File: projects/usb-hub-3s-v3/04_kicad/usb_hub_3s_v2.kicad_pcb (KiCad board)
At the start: 4 copper layers, 130 x 92 mm, 114 parts, among them J1 C98732, J2 C503996, J3 C503996, J4 C503996, J5 C5337088, Q1 C2760089, Q2 C404363, Q3 C404363, Q4 C404363, Q5 C404363, Q6 C2760089, Q7 C78284, SW1 C2939728, U10 C7519, U11 C13755, U12 C7519, U2 C13755, U3 C130056, U4 C130056, U5 C130056, U6 C473910, U7 C473910, U8 C7519, U9 C7519

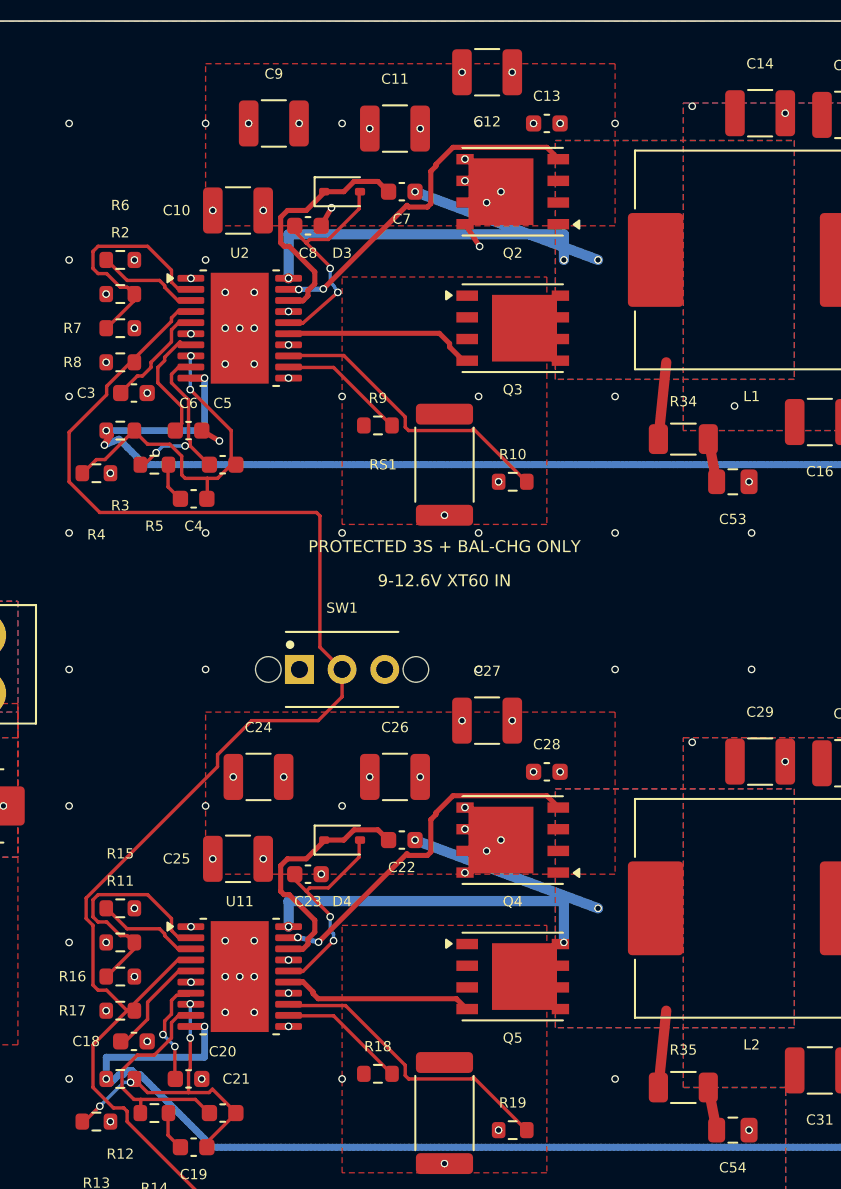
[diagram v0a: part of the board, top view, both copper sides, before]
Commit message: usb-hub-3s-v3 v1.3 gate (ii-b): R30 wrong-part fix (C25803) + full regen [source commit S]
R30 (Q6 gate pull-up QG->PMID) was the SECOND wrong-part of the v1.2
class: tscircuit value-resolved it to C2933195 = FRC0603F3091TS =
catalog 3.09k while labeled 100k (v1.2 SUPERSEDED addendum 688a8af).
Fix: bake C25803 (UNI-ROYAL 0603WAF1003T5E, ledger-verified 100k 1%
0603, JLC Basic) in the tsx — the same code R1/R8/R17 already resolve
to, so the BOM row merges (44 -> 43 grouped lines).

Q6 margins re-derived at the REAL 100k (AON6403 STATIC table):
OFF/back-feed |Vgs| ~ 60 mV = (Q7 Idss 0.5uA + Q6 IGSS 0.1uA) x 100k,
20x below |Vgs(th)|min 1.2V -> blocks (RT-T4 holds); ON Vgs = -5.35V
fully enhanced; pull-up waste 54uA vs ~1.7mA at the wrong 3.09k.

Full regen (the killed-mid-run prior outputs were re-run from scratch):
tsci build -> grid converter (110/110 FPID, ERC 0) -> netlist (the
15:54 export was stale, pre-R30) -> E-INV 24/24 -> rebuild_fast
(promoted chain; run #1 gave DRC 3/0/0 — taps/stitch is stochastic on
the first pass after a converter regen, run #2 = 0/0/0, both times this
family) -> fab/PDF/STEP/twin regen -> restaged 07_releases/v1.3.

Gates (MEASURED, restaged archive): DRC 0/0/0 severity-all +
refill-zones + parity; ERC 0; E-INV 24/24; bom_source_check PASS incl.
the semantic value-vs-ledger leg (the R30 VALUE-MISMATCH is gone); BOM
delta vs sealed v1.2 = EXACTLY {R12 C2933210->C2984354, D5
C140903->C113976, R30 C2933195->C25803} diff-verified; CPL 108 with
SW1+F1 absent; jlc_twin 88 OK / 235 exit 0, R30 fit 0.08mm
MODEL-REG-OK, zero unadjudicated criticals; policy_audit FAIL=1 =
M-REL only (stale MANIFEST sha table, re-stamped next commit per the
2-commit seal); freshness: sole finding = same pre-stamp disagreement.

Scoped verification (fix-pass leg): targeted delta confirmation
archived at 08_reviews/2026-07-23_v1.3_fix_confirmation.md (PASS);
zero-context fresh lens over the curated staging archive: VERDICT ORDER, no P0/no P1, 6 P2s (dispositioned; 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
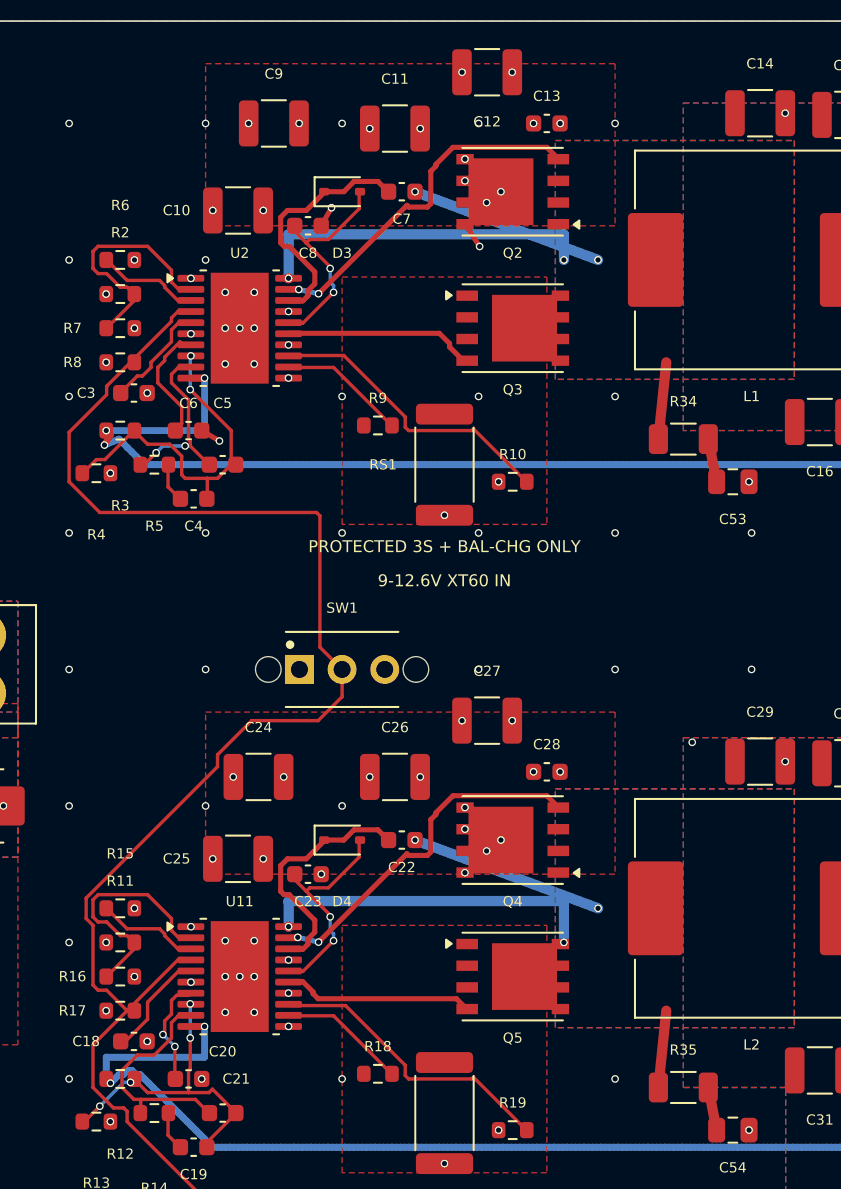
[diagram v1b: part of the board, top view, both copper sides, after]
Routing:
- net 5VA: vias 8 -> 6
